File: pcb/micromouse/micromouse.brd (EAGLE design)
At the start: 80 x 115 mm, 76 parts, among them IC1 LM2575-5.0WU-(TR), IC2 LM2575-3.3WU-(TR), IC3 DSPIC33FJ64MC804-PT, IC4 L293D, Y1 7.3728MHz

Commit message: cosmetics
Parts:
- flipped R8 to the bottom
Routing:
- net BTN_2: track 56.7 -> 56.6 mm, vias 4 -> 3
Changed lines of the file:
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@@
 <dimension x1="29.5" y1="111" x2="26.5" y2="111" x3="28" y3="106.5" textsize="1.778" layer="47" dtype="vertical"/>
 <dimension x1="50.5" y1="111" x2="53.5" y2="111" x3="52" y3="106.5" textsize="1.778" layer="47"/>
-<text x="55.3212" y="98.1202" size="0.8128" layer="21" rot="R270">R8</text>
+<text x="56.1848" y="98.1202" size="0.8128" layer="22" rot="MR270">R8</text>
 <text x="31.877" y="90.5764" size="0.8128" layer="22" rot="MR0">C12</text>
 <text x="20.574" y="13.462" size="0.8128" layer="21" rot="R180">C1</text>
@@
 <attribute name="VALUE" x="28.1178" y="90.6018" size="1.27" layer="27" ratio="10"/>
 </element>
-<element name="R8" library="rcl" library_urn="urn:adsk.eagle:library:334" package="R0805" package3d_urn="urn:adsk.eagle:package:23553/2" value="10kR" x="57.15" y="97.346" smashed="yes" rot="R270">
-<attribute name="POPULARITY" value="86" x="67.31" y="97.346" size="1.778" layer="27" rot="R270" display="off"/>
-<attribute name="SPICEPREFIX" value="R" x="67.31" y="97.346" size="1.778" layer="27" rot="R270" display="off"/>
-<attribute name="VALUE" x="54.61" y="97.981" size="1.27" layer="27" rot="R270"/>
+<element name="R8" library="rcl" library_urn="urn:adsk.eagle:library:334" package="R0805" package3d_urn="urn:adsk.eagle:package:23553/2" value="10kR" x="57.15" y="97.346" smashed="yes" rot="MR270">
+<attribute name="POPULARITY" value="86" x="46.99" y="97.346" size="1.778" layer="28" rot="MR270" display="off"/>
+<attribute name="SPICEPREFIX" value="R" x="46.99" y="97.346" size="1.778" layer="28" rot="MR270" display="off"/>
+<attribute name="VALUE" x="59.69" y="97.981" size="1.27" layer="28" rot="MR270"/>
 </element>
 <element name="S4" library="switch-omron" library_urn="urn:adsk.eagle:library:377" package="B3F-10XX" package3d_urn="urn:adsk.eagle:package:27496/1" value="B3F-1000" x="50.0906" y="95.6688" smashed="yes" rot="R180">
@@
 <wire x1="53.086" y1="68.326" x2="48.006" y2="68.326" width="0.254" layer="1"/>
 <wire x1="53.34" y1="68.58" x2="55.118" y2="70.358" width="0.254" layer="16"/>
-<via x="55.118" y="96.012" extent="1-16" drill="0.35"/>
-<wire x1="55.118" y1="96.012" x2="53.3418" y2="97.7882" width="0.254" layer="1"/>
-<wire x1="53.3418" y1="97.7882" x2="53.3418" y2="97.9294" width="0.254" layer="1"/>
-<wire x1="55.118" y1="70.358" x2="55.118" y2="96.012" width="0.254" layer="16"/>
-<wire x1="57.15" y1="96.396" x2="56.766" y2="96.012" width="0.254" layer="1"/>
-<wire x1="55.118" y1="96.012" x2="56.766" y2="96.012" width="0.254" layer="1"/>
 <wire x1="46.482" y1="63.246" x2="44.7548" y2="61.5188" width="0.254" layer="16"/>
 <wire x1="44.7548" y1="61.5188" x2="43.3832" y2="61.5188" width="0.254" layer="16"/>
@@
 <wire x1="38.2524" y1="62.8904" x2="38.862" y2="63.5" width="0.254" layer="16"/>
 <wire x1="38.862" y1="63.5" x2="41.402" y2="63.5" width="0.254" layer="16"/>
+<wire x1="53.3418" y1="97.9294" x2="55.118" y2="96.1532" width="0.254" layer="16"/>
+<wire x1="55.118" y1="70.358" x2="55.118" y2="96.1532" width="0.254" layer="16"/>
+<wire x1="55.118" y1="96.1532" x2="56.9072" y2="96.1532" width="0.254" layer="16"/>
+<wire x1="56.9072" y1="96.1532" x2="57.15" y2="96.396" width="0.254" layer="16"/>
 </signal>
 <signal name="VCAP/VDDCORE">

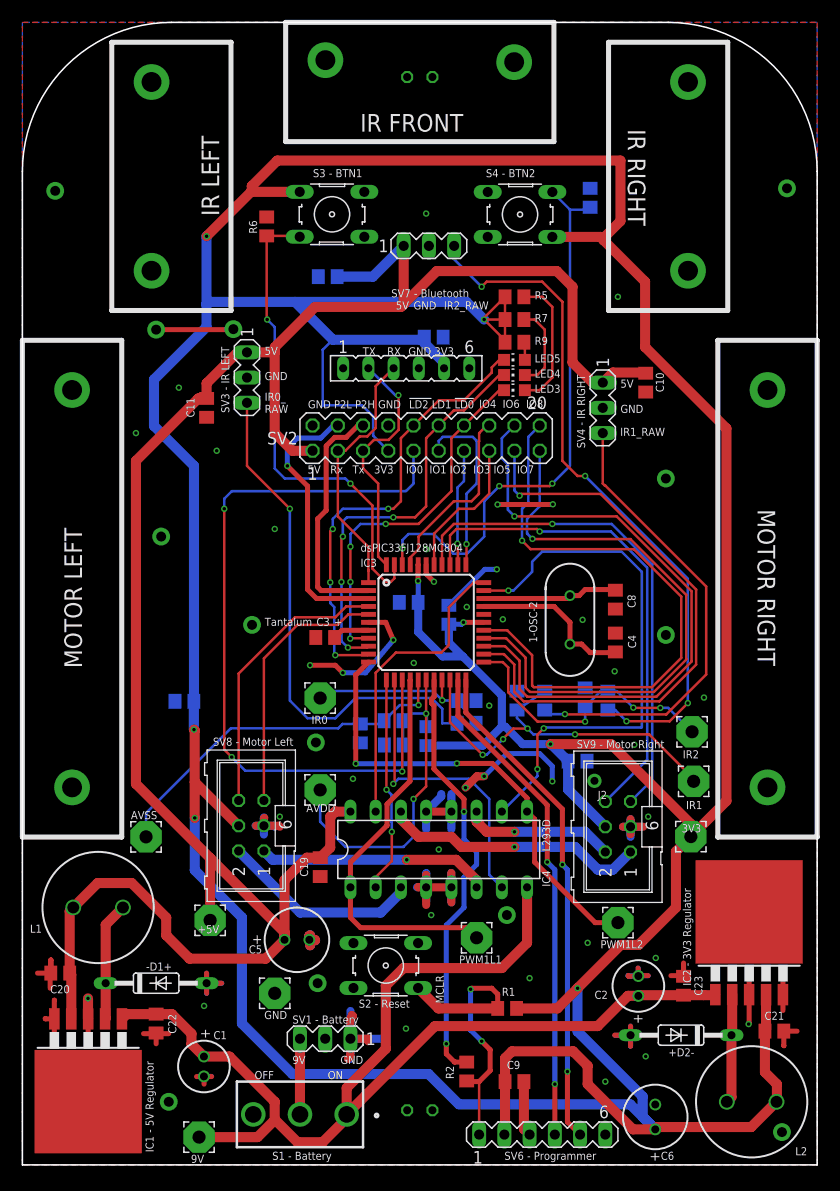
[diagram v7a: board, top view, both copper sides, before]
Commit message: Move front IR sensor more to the center and fixthe positioning of silk writing.
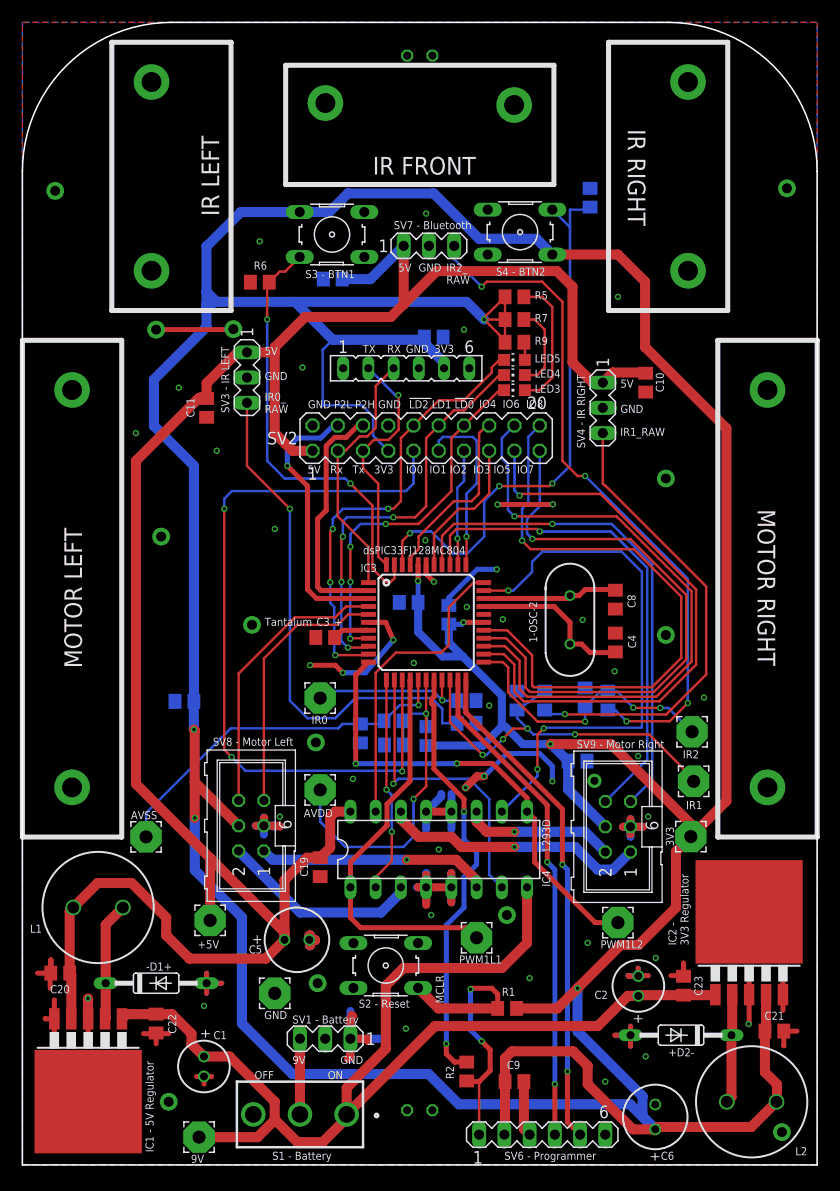
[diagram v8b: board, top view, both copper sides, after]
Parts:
- moved R6 5.66 mm to (23.9, 88.8), turned to 0 degrees
- moved LED1 2.16 mm to (40.0, 111.7)
- moved S3 2.03 mm to (31.2, 93.6)
- moved S4 1.78 mm to (50.1, 93.9)
- moved C12 0.57 mm to (31.2, 89.2)
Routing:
- net +3V3: track 514.5 -> 496.0 mm, vias 8 -> 7
- net BTN_1: track 49.1 -> 45.3 mm
- net GND: track 168.1 -> 168.6 mm, vias 62 -> 65
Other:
- board text added: "IR2_ RAW"
- board text added: "Micromouse SS2022 "THE MICROMOUSER" Ludwig Stumpp Franz Kaschner Marwan Shalaby Hatem Elsayed"
- board text removed: "IR2_RAW"
- board text removed: "J2"
- board text removed: "Micromouse SS2022 Ludwig Stumpp Franz Kaschner Marwan Shalaby Hatem Elsayed"
